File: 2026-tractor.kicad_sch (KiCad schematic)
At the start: 0 parts

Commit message: Testing commits
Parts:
- added U1: 4060, symbol 4xxx:4060
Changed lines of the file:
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@@
 	(generator_version "9.0")
 	(paper "A4")
+	(symbol
+		(lib_id "4xxx:4060")
+		(at 95.25 73.66 0)
+		(unit 1)
+		(exclude_from_sim no)
+		(in_bom yes)
+		(on_board yes)
+		(dnp no)
+		(fields_autoplaced yes)
+		(property "Reference" "U1"
+			(at 97.3933 53.34 0)
+			(effects
+				(font
+					(size 1.27 1.27)
+				)
+				(justify left)
+			)
+		)
+		(property "Value" "4060"
+			(at 97.3933 55.88 0)
+			(effects
+				(font
+					(size 1.27 1.27)
+				)
+				(justify left)
+			)
+		)
+		(property "Footprint" ""
+			(at 95.25 76.2 0)
+			(effects
+				(font
+					(size 1.27 1.27)
+				)
+				(hide yes)
+			)
+		)
+		(property "Datasheet" "https://www.st.com/resource/en/datasheet/m74hc4060.pdf"
+			(at 95.25 78.74 0)
+			(effects
+				(font
+					(size 1.27 1.27)
+				)
+				(hide yes)
+			)
+		)
+		(property "Description" "Binary counter (14-stages) and oscillator"
+			(at 95.25 73.66 0)
+			(effects
+				(font
+					(size 1.27 1.27)
+				)
+				(hide yes)
+			)
+		)
+		(pin "1"
+		)
+		(pin "10"
+		)
+		(pin "7"
+		)
+		(pin "4"
+		)
+		(pin "9"
+		)
+		(pin "8"
+		)
+		(pin "14"
+		)
+		(pin "13"
+		)
+		(pin "11"
+		)
+		(pin "12"
+		)
+		(pin "3"
+		)
+		(pin "15"
+		)
+		(pin "16"
+		)
+		(pin "6"
+		)
+		(pin "5"
+		)
+		(pin "2"
+		)
+		(instances
+			(project ""
+				(path "/614b9759-e400-4d9a-b999-e6a52a22018a"
+					(reference "U1")
+					(unit 1)
+				)
+			)
+		)
+	)
 	(sheet_instances
 		(path "/"

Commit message: lighting started
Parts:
- added BT1: Battery_Cell, symbol Device:Battery_Cell
- added F1: Fuse, symbol Device:Fuse
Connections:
- new net: BT1.1 (+), F1.1
- new net GND: BT1.2 (-)

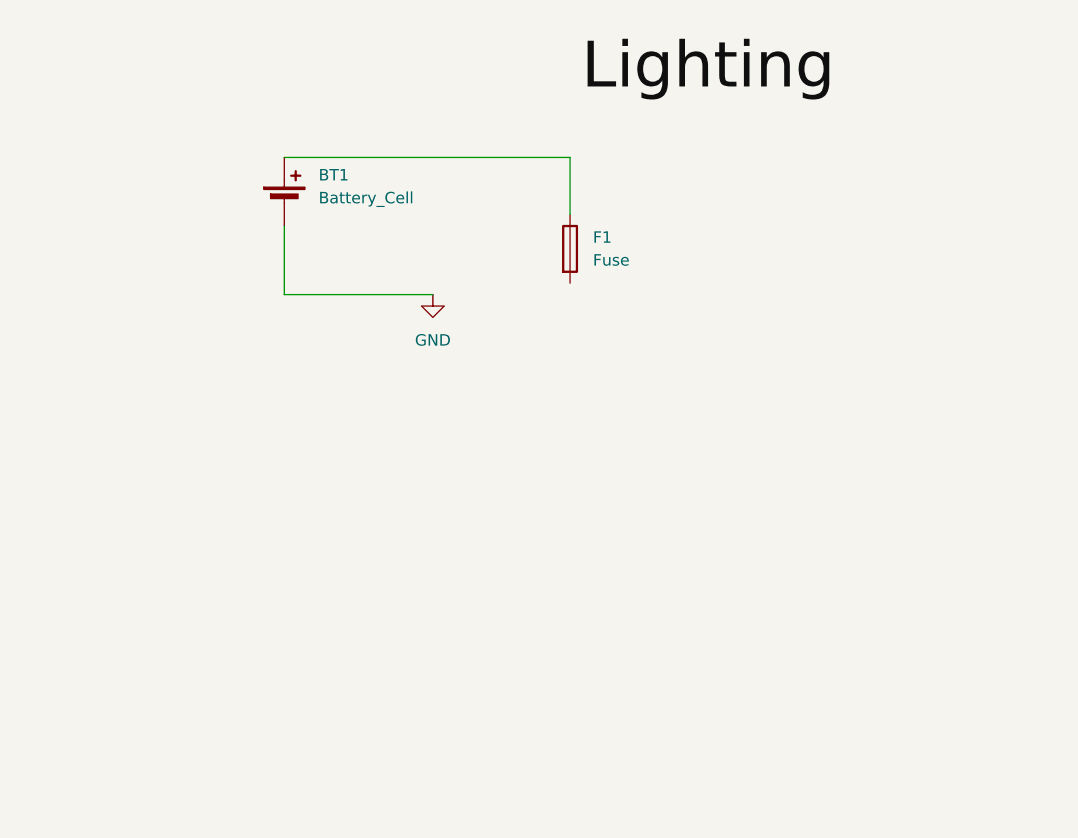
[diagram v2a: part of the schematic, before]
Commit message: lighting: breaks and flashers
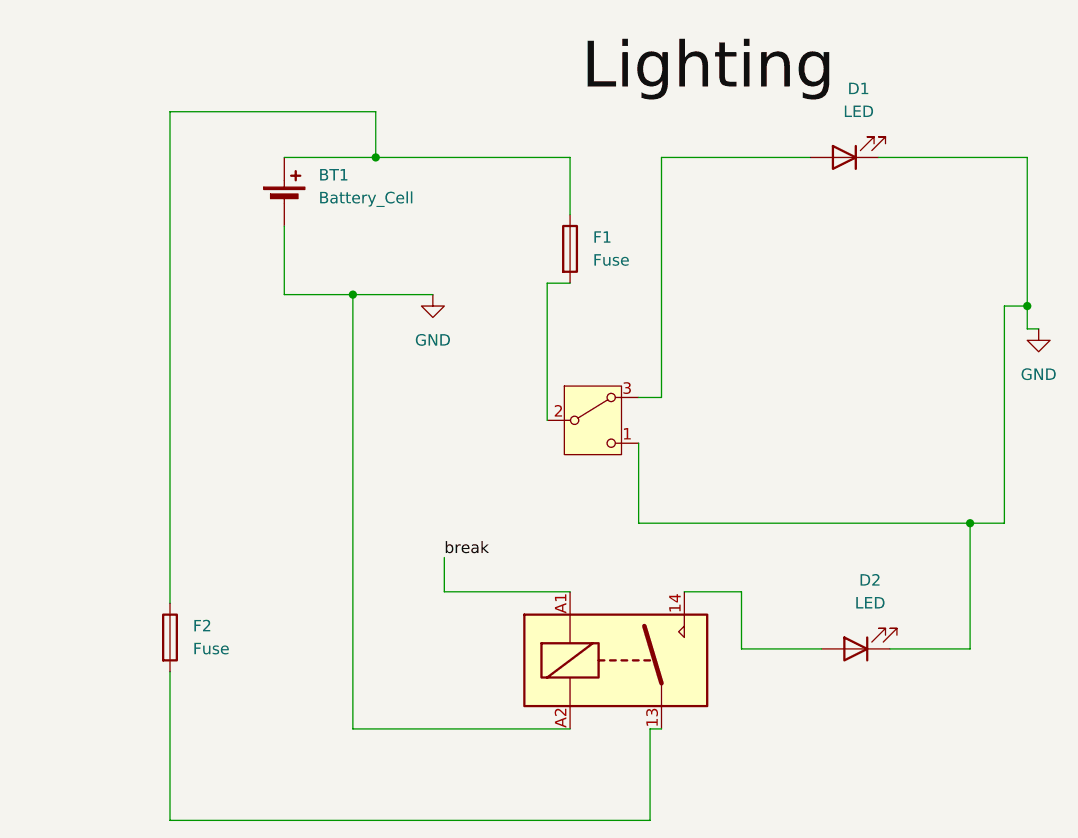
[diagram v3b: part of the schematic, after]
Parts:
- added D1, D2: LED, symbol Device:LED
- added F2: Fuse, symbol Device:Fuse
- added K1: Fujitsu_FTR-LYAA005x, Relay_THT:Relay_SPST-NO_Fujitsu_FTR-LYAA005x_FormA_Vertical, symbol Relay:Fujitsu_FTR-LYAA005x
- added SW1: SW_Nidec_CAS-120A1, Button_Switch_SMD:Nidec_Copal_CAS-120A, symbol Switch:SW_Nidec_CAS-120A1
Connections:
- net GND: now also D1.1 (K), D2.1 (K), K1.A2, SW1.1 (C)
- net at BT1.1 (+), F1.1: now also F2.1
- net at F1.2: now also SW1.2 (B)
- new net: D1.2 (A), SW1.3 (A)
- new net: D2.2 (A), K1.14
- new net: F2.2, K1.13
- new net break: K1.A1

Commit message: Lighitng Schematic completed
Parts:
- added BT2: Battery_Cell, symbol Device:Battery_Cell
- added D3: LED Strip, symbol Device:LED
- added D4: Break Light, symbol Device:LED
- added D5: Tail Light, symbol Device:LED
- added D6: HeadLight, symbol Device:LED
- added F3, F4, F5, F6, F7: Fuse, symbol Device:Fuse
- added K2: Fujitsu_FTR-LYAA005x, Relay_THT:Relay_SPST-NO_Fujitsu_FTR-LYAA005x_FormA_Vertical, symbol Relay:Fujitsu_FTR-LYAA005x
- added SW2, SW3, SW4: SW_Nidec_CAS-120A1, Button_Switch_SMD:Nidec_Copal_CAS-120A, symbol Switch:SW_Nidec_CAS-120A1
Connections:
- net GND: now also BT2.2 (-), D3.1 (K), D4.1 (K), D5.1 (K), D6.1 (K), K2.GND, SW2.1 (C), SW3.1 (C), SW4.1 (C)
- new net: BT2.1 (+), F3.1, F4.1, F5.1, F6.1, F7.1
- new net: D3.2 (A), SW4.3 (A)
- new net: F3.2, SW4.2 (B)
- new net: D6.2 (A), SW2.3 (A)
- new net: D5.2 (A), F5.2, SW2.2 (B), SW3.3 (A)
- new net: F7.2, K2.Power
- new net: D4.2 (A), K2.LED
- new net: F4.2, SW3.2 (B)
- new net Break Sensor: F6.2, K2.Sensor
